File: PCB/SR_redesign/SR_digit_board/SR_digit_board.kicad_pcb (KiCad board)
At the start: 2 copper layers, 82 parts, among them J1 Conn_02x07_Counter_Clockwise, J2 Conn_01x09, J3 Conn_01x10, J4 Conn_01x09, Q1 MPSA92-AP, Q10 MPSA42-AP, Q11 MPSA42-AP, Q12 MPSA42-AP, Q2 MPSA92-AP, Q3 MPSA92-AP, Q4 MPSA42-AP, Q5 MPSA42-AP, Q6 MPSA42-AP, Q7 MPSA92-AP, Q8 MPSA92-AP, Q9 MPSA92-AP, U1 74141, U2 74141, U3 74141, U4 SN74HC595N, U5 SN74HC595N, U6 SN74HC595N, U7 ATMEGA328PB-AU

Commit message: SR redesign: hour and minute sections have vertical ribbon headers. need to rearrange seconds. putting in breaks in the board but maybe that's a dumb idea idk
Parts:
- removed TP10, TP11, TP12, TP14, TP17, TP18, TP19, TP22, TP24, TP4, TP5, TP6: RCU-0C, digikey-footprints:PROBE_PAD_0603
- U1, U2: moved to B.Cu
- moved R17 202.1 mm to (34.3, 137.9), turned to -90 degrees
- moved Q10 193.9 mm to (39.2, 135.3), turned to -90 degrees
- moved Q4 188.8 mm to (60.5, 135.3), turned to -90 degrees
- moved R4 185.2 mm to (54.7, 137.9), turned to 90 degrees
- moved R10 181.9 mm to (54.8, 132.4)
- moved R5 177.8 mm to (65.4, 137.9), turned to 90 degrees
- moved R22 173.7 mm to (44.8, 133.8), turned to 0 degrees
- moved J4 170.0 mm to (238.6, 100.8)
- moved Q12 170.0 mm to (213.3, 135.1)
- moved Q3 170.0 mm to (236.8, 135.1)
- moved Q6 170.0 mm to (226.6, 135.1)
- moved Q9 170.0 mm to (200.7, 135.0)
- moved R12 170.0 mm to (219.5, 136.7)
- moved R15 170.0 mm to (198.5, 129.8)
- moved R20 170.0 mm to (206.9, 136.4)
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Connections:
- U5 pad 14: Net-(TP1-Pad1) -> SerialMin
- U5 pad 9: Net-(TP4-Pad1) -> SerialHr
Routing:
- net Vtube: track 47.3 -> 195.7 mm
- net +5V: track 90.8 -> 237.5 mm
- net Net-(D3-Pad10): track 0.00 -> 95.6 mm
- net Net-(D1-Pad10): track 0.00 -> 95.1 mm
- net Net-(D3-Pad3): track 0.00 -> 81.3 mm
- net Net-(D1-Pad3): track 0.00 -> 80.7 mm
- net Net-(U2-Pad6): track 0.00 -> 74.9 mm
- net Net-(U1-Pad6): track 0.00 -> 74.5 mm
- net Net-(U2-Pad4): track 0.00 -> 73.1 mm
- net Net-(U1-Pad4): track 0.00 -> 72.5 mm
- net Net-(J2-Pad6): track 16.3 -> 88.4 mm
- net Net-(J2-Pad7): track 11.9 -> 82.8 mm
- net Net-(U2-Pad7): track 0.00 -> 68.9 mm
- net Net-(U1-Pad7): track 0.00 -> 68.7 mm
- net Net-(U2-Pad3): track 0.00 -> 66.8 mm
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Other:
- board outline added: 234 x 84 mm

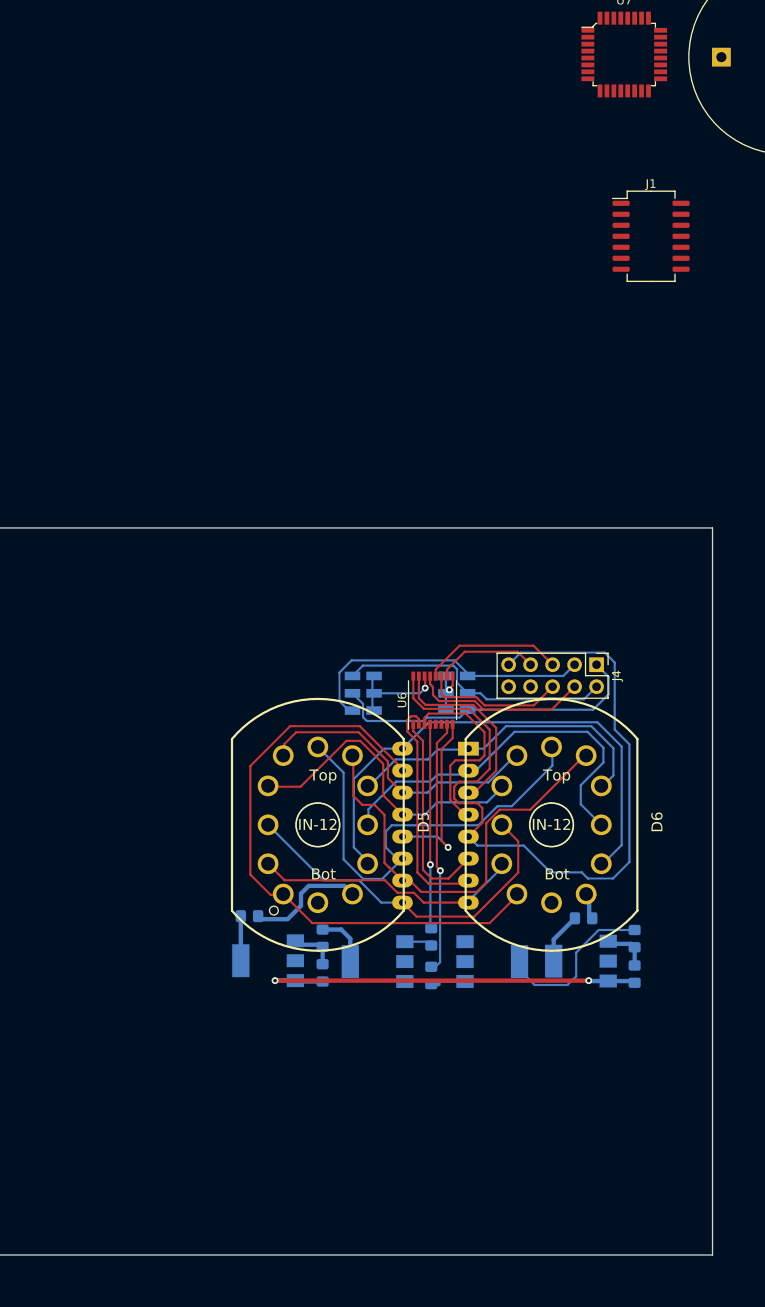
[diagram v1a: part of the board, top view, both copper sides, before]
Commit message: SR redesign - added buttons. copypasted seconds
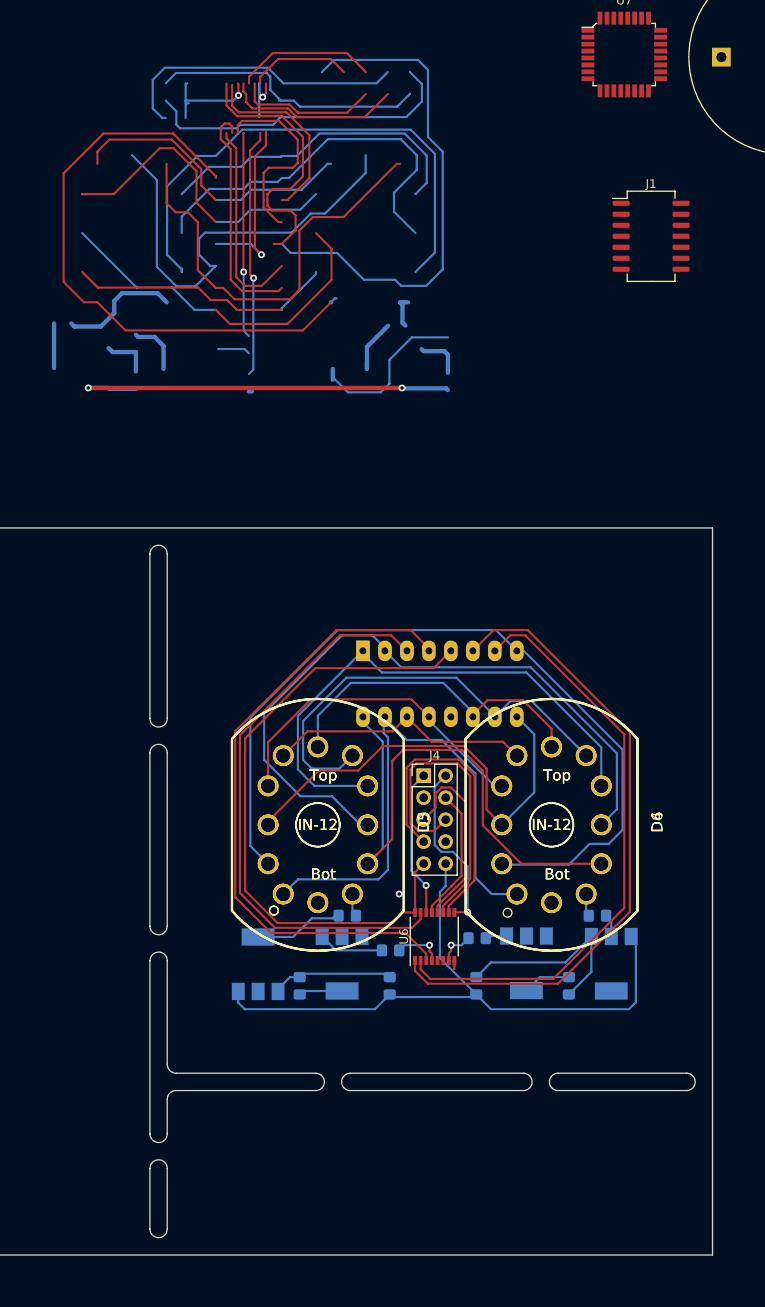
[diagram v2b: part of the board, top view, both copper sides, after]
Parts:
- removed TP1, TP13, TP15, TP16, TP2, TP20, TP21, TP23, TP3, TP7, TP8, TP9: RCU-0C, digikey-footprints:PROBE_PAD_0603
- added D3: IN-12, nixies-us:nixies-us-IN-12-DSUB, F.Cu at (206.4, 119.3)
- added D4: IN-12, nixies-us:nixies-us-IN-12-DSUB, F.Cu at (233.4, 119.3)
- moved U6 27.3 mm to (219.9, 132.2)
- moved J4 23.7 mm to (218.6, 113.6), turned to 0 degrees
- moved R8 18.3 mm to (224.7, 137.9)
- moved U3 16.6 mm to (211.6, 99.2), turned to -90 degrees
- moved R15 11.3 mm to (209.8, 129.8)
- moved R9 9.35 mm to (235.4, 137.9)
- moved R20 7.89 mm to (214.7, 137.9)
- moved R12 6.82 mm to (224.8, 132.4), turned to 180 degrees
- moved R21 6.11 mm to (204.3, 137.9)
- moved R24 4.95 mm to (214.8, 133.8), turned to 0 degrees
- moved Q12 4.11 mm to (209.2, 135.3), turned to -90 degrees
- moved Q6 3.96 mm to (230.5, 135.3), turned to -90 degrees
- moved Q3 3.51 mm to (240.3, 135.3), turned to -90 degrees
- moved R3 1.63 mm to (238.7, 129.8), turned to 180 degrees
- moved Q9 1.22 mm to (199.5, 135.4), turned to 90 degrees
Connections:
- U4 pad 14: Net-(TP4-Pad1) -> Net-(U4-Pad14)
- U5 pad 14: SerialMin -> Net-(U5-Pad14)
- U5 pad 9: SerialHr -> Net-(U4-Pad14)
- U6 pad 14: Net-(U6-Pad14) -> unconnected-(U6-Pad14)
- U6 pad 9: Net-(TP1-Pad1) -> Net-(U5-Pad14)
- U7 pad 23: unconnected-(U7-Pad23) -> Switch0
- U7 pad 24: unconnected-(U7-Pad24) -> Switch1
- U7 pad 25: unconnected-(U7-Pad25) -> Switch2
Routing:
- net Net-(D3-Pad10): track 95.6 -> 191.2 mm
- net Net-(D3-Pad3): track 81.3 -> 162.6 mm
- net Net-(U3-Pad6): track 23.8 -> 98.6 mm
- net Vtube: track 195.7 -> 270.2 mm
- net +5V: track 237.5 -> 310.8 mm
- net Net-(U3-Pad4): track 22.8 -> 95.9 mm
- net Net-(U3-Pad7): track 27.0 -> 95.9 mm
- net Net-(U3-Pad3): track 22.0 -> 88.8 mm
- net Net-(D3-Pad2): track 66.0 -> 132.0 mm
- net Net-(D3-Pad4): track 62.4 -> 124.9 mm
- net Net-(D3-Pad11): track 62.0 -> 124.1 mm
- net Net-(U4-Pad14): track 0.00 -> 59.0 mm
- net Net-(D3-Pad9): track 53.2 -> 106.5 mm
- net Net-(D3-Pad5): track 51.3 -> 102.6 mm
- net Net-(U5-Pad14): track 0.00 -> 41.1 mm, vias 0 -> 1
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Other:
- outline, holes or cut-outs redrawn

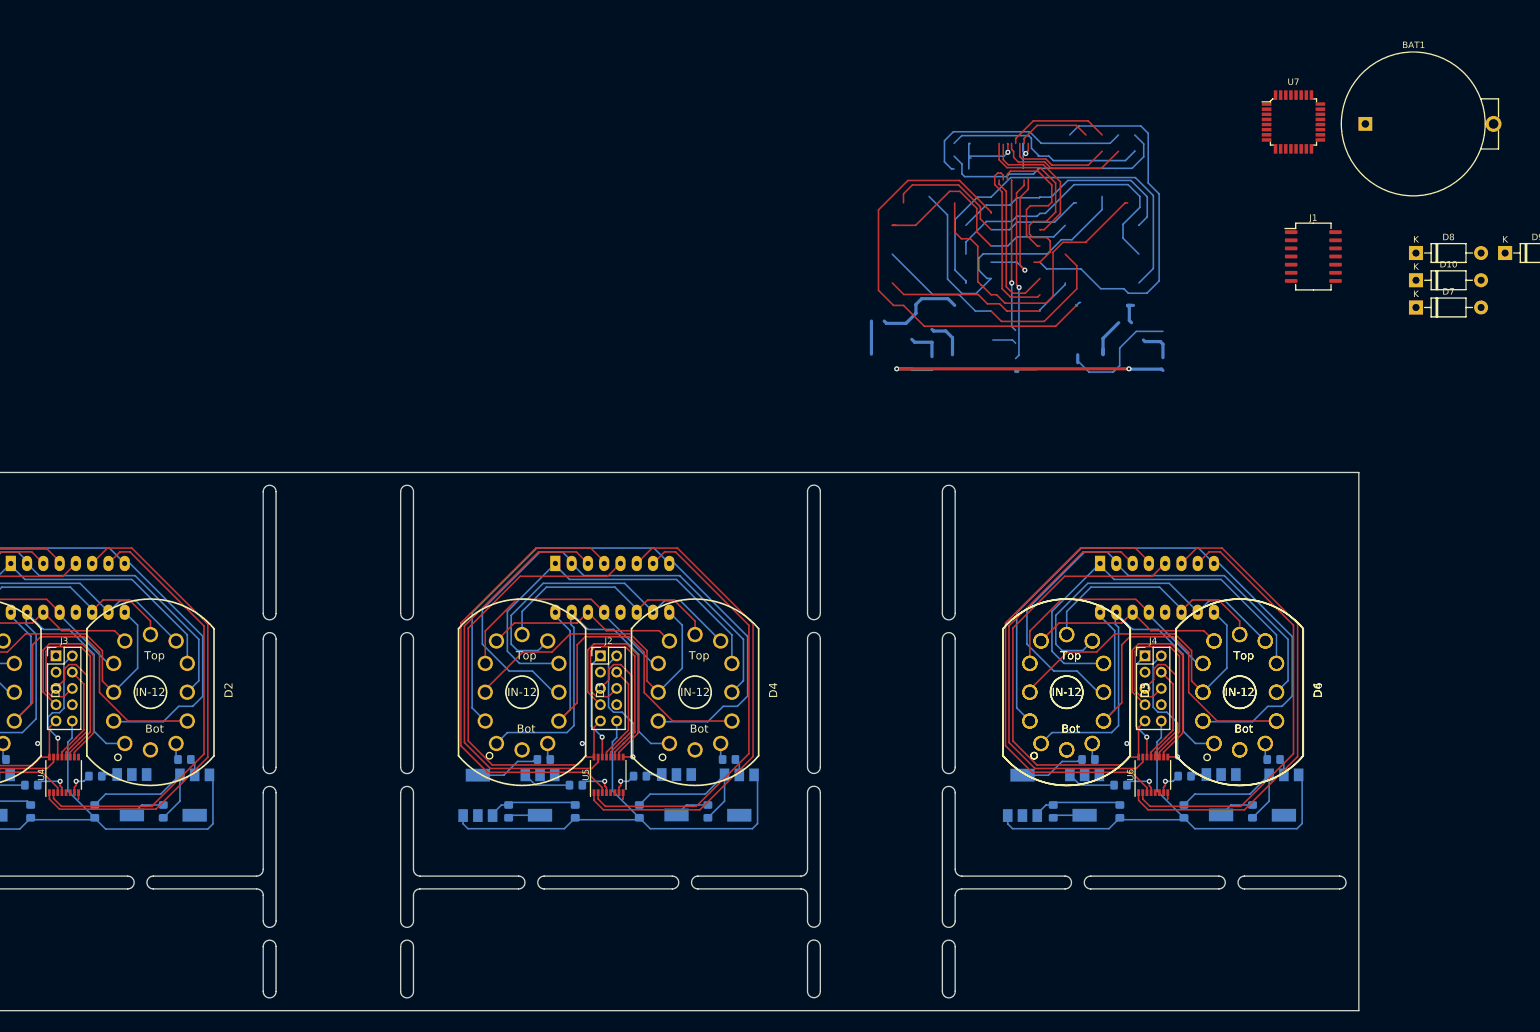
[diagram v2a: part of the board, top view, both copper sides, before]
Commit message: SR redesign - added atmega support components, still need xtal footprint
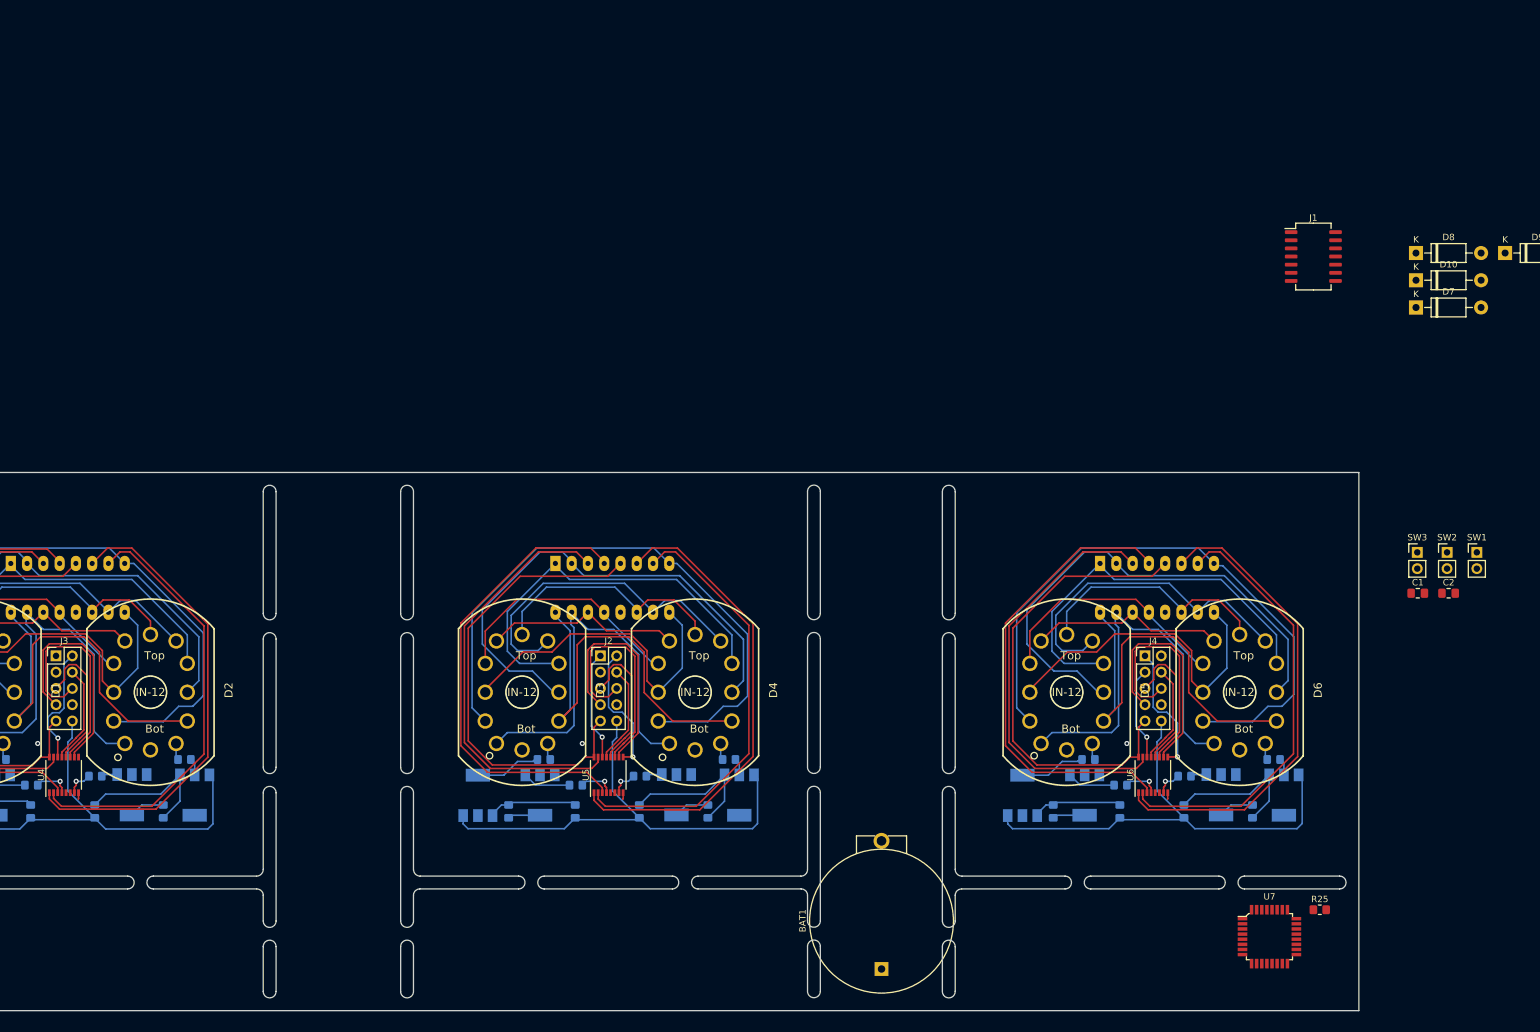
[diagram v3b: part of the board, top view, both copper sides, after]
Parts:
- removed the D3 at (206.4, 119.3)
- removed the D4 at (233.4, 119.3)
- added C1: 22p, Capacitor_SMD:C_0805_2012Metric_Pad1.18x1.45mm_HandSolder, F.Cu at (261.2, 103.8)
- added C2: 22p, Capacitor_SMD:C_0805_2012Metric_Pad1.18x1.45mm_HandSolder, F.Cu at (266.0, 103.8)
- added R25: 15k, Resistor_SMD:R_0805_2012Metric_Pad1.20x1.40mm_HandSolder, F.Cu at (245.9, 153.2)
- added SW1: SW_Push_SPDT, Connector_PinHeader_2.54mm:PinHeader_1x02_P2.54mm_Vertical, F.Cu at (270.4, 97.5)
- added SW2: SW_Push_SPDT, Connector_PinHeader_2.54mm:PinHeader_1x02_P2.54mm_Vertical, F.Cu at (265.8, 97.5)
- added SW3: SW_Push_SPDT, Connector_PinHeader_2.54mm:PinHeader_1x02_P2.54mm_Vertical, F.Cu at (261.1, 97.5)
- moved BAT1 152.0 mm to (177.5, 162.5), turned to 90 degrees
- moved U7 127.2 mm to (238.1, 157.4)
- turned R21 to -90 degrees
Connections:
- U7 pad 13: unconnected-(U7-Pad13) -> Net-(U7-Pad13)
- U7 pad 14: unconnected-(U7-Pad14) -> Net-(U7-Pad14)
- U7 pad 18: unconnected-(U7-Pad18) -> Net-(D10-Pad1)
- U7 pad 29: unconnected-(U7-Pad29) -> Net-(R25-Pad1)
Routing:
- net Net-(D3-Pad10): track 191.2 -> 95.8 mm
- net +5V: track 310.8 -> 220.0 mm
- net Net-(D3-Pad3): track 162.6 -> 81.3 mm
- net Net-(D3-Pad2): track 132.0 -> 66.0 mm
- net Net-(D5-Pad10): track 30.9 -> 95.9 mm
- net Net-(D3-Pad4): track 124.9 -> 62.4 mm
- net Net-(D3-Pad11): track 124.1 -> 62.0 mm
- net Net-(D3-Pad9): track 106.5 -> 53.2 mm
- net Net-(D3-Pad5): track 102.6 -> 51.3 mm
- net Vtube: track 270.2 -> 222.9 mm, vias 2 -> 0
- net Net-(U4-Pad14): track 59.0 -> 18.6 mm
- net Net-(D3-Pad8): track 79.7 -> 39.8 mm
- net Net-(D3-Pad6): track 77.0 -> 38.5 mm
- net Net-(D5-Pad3): track 44.6 -> 81.3 mm
- net SerialSec: track 34.3 -> 0.00 mm, vias 0 -> 1
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
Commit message: SR redesign - most of the layout seems to be there. need a power supply
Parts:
- removed D7, D9: 1N4001, Diode_THT:D_DO-41_SOD81_P10.16mm_Horizontal
- added J4: Conn_01x09, Connector_PinHeader_2.54mm:PinHeader_2x05_P2.54mm_Vertical, F.Cu at (176.1, 113.7)
- added Y1: 16MHz, Crystal:Crystal_HC18-U_Vertical, B.Cu at (217.2, 154.3)
- C1, C2: moved to B.Cu
- moved D8 125.2 mm to (201.6, 161.0), turned to 180 degrees
- moved D10 124.3 mm to (201.6, 164.2), turned to 180 degrees
- moved J1 109.9 mm to (234.2, 160.7), turned to 180 degrees
- moved SW1 94.7 mm to (205.8, 166.8), turned to 180 degrees
- moved SW2 89.9 mm to (208.5, 166.7), turned to 180 degrees
- moved SW3 85.4 mm to (211.2, 166.7), turned to 180 degrees
- moved C1 70.8 mm to (212.5, 155.3), turned to 90 degrees
- moved C2 64.7 mm to (226.8, 155.3), turned to 90 degrees
- moved R25 23.8 mm to (225.6, 165.7)
- moved U7 20.0 mm to (218.4, 161.0), turned to 180 degrees
- moved BAT1 16.3 mm to (177.3, 146.2), turned to -90 degrees
- moved D5 0.10 mm to (206.4, 119.4)
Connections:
- D10 pad 1: Net-(D10-Pad1) -> ORpower
- D8 pad 1: Net-(D10-Pad1) -> ORpower
- J1 pad 6: Net-(D7-Pad1) -> ORpower
- SW1 pad 1: unconnected-(SW1-Pad1) -> GND
- SW2 pad 1: unconnected-(SW2-Pad1) -> GND
- SW3 pad 1: unconnected-(SW3-Pad1) -> GND
- U4 pad 14: Net-(U4-Pad14) -> SerialHr
- U5 pad 14: Net-(U5-Pad14) -> SerialMin
- U5 pad 9: Net-(U4-Pad14) -> SerialHr
- U6 pad 9: Net-(U5-Pad14) -> SerialMin
- U7 pad 18: Net-(D10-Pad1) -> ORpower
- U7 pad 4: Net-(D10-Pad1) -> ORpower
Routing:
- net +5V: track 220.0 -> 359.6 mm
- net Net-(J2-Pad4): track 46.3 -> 145.1 mm
- net Net-(J2-Pad5): track 66.6 -> 162.8 mm
- net Net-(J2-Pad7): track 106.4 -> 194.9 mm
- net Net-(J2-Pad6): track 108.1 -> 195.2 mm
- net SerialSec: track 0.00 -> 80.3 mm
- net ORpower: track 0.00 -> 49.3 mm, vias 0 -> 2
- net Vtube: track 222.9 -> 266.8 mm
- net Net-(J1-Pad2): track 0.00 -> 22.7 mm
- net SerialMin: track 17.1 -> 37.5 mm
- net Net-(U5-Pad14): track 20.3 -> 0.00 mm
- net SerialHr: track 20.2 -> 38.8 mm
- net Net-(U4-Pad14): track 18.6 -> 0.00 mm
- net Vbatt: track 0.00 -> 18.2 mm
- net Net-(J1-Pad13): track 0.00 -> 15.5 mm, vias 0 -> 2
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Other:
- board size 234 x 84 mm -> 234.1 x 84 mm
